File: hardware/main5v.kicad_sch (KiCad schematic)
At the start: 12 parts, among them U701 TPS56837RPAR

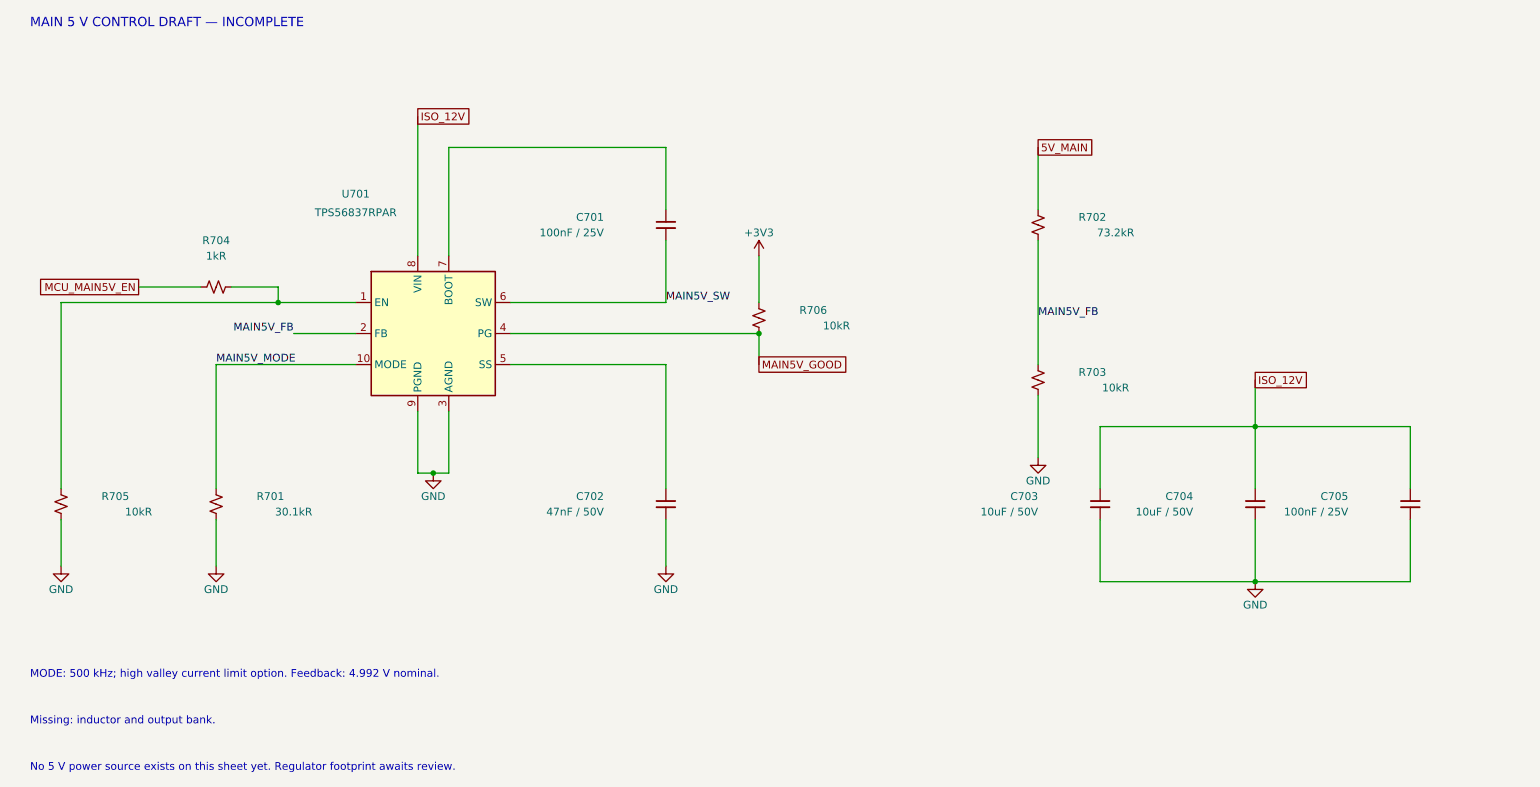
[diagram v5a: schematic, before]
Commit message: Capture main 5 V inductor and local output capacitor bank
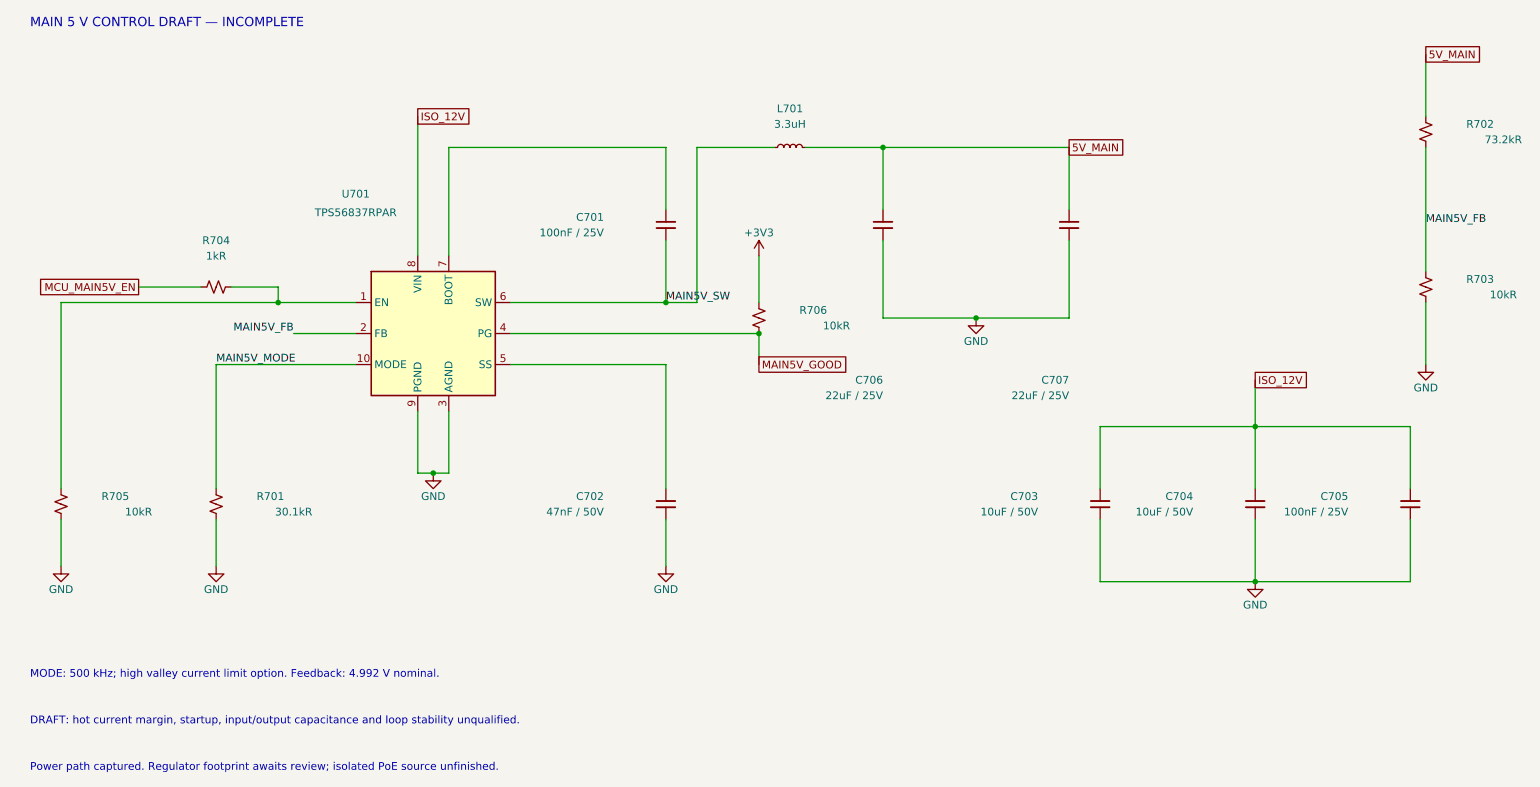
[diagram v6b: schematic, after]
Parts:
- added C706, C707: 22uF / 25V, Capacitor_SMD:C_1210_3225Metric, symbol Device:C_Small
- added L701: 3.3uH, Inductor_SMD:L_Coilcraft_XAL7070-XXX, symbol Device:L_Small
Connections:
- net 5V_MAIN: now also C706.1, C707.1, L701.2
- net GND: now also C706.2, C707.2
- net MAIN5V_SW: now also L701.1
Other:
- note added: "DRAFT: hot current margin, startup, input/output capacitance and loop stability unqualified."
- note added: "Power path captured. Regulator footprint awaits review; isolated PoE source unfinished."
- note removed: "Missing: inductor and output bank."
- note removed: "No 5 V power source exists on this sheet yet. Regulator footprint awaits review."
- moved on the sheet: R702, R703

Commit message: Complete appliance engineering schematic capture
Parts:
- U701: Qualification Footprint pending review; incomplete power path -> Power path captured; RPA land pattern and electrical qualif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
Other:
- note added: "MAIN 5 V CONTROL — ENGINEERING CAPTURE"
- note added: "Power path captured. Regulator footprint, stability and thermal release remain pending."
- note removed: "MAIN 5 V CONTROL DRAFT — INCOMPLETE"
- note removed: "Power path captured. Regulator footprint awaits review; isolated PoE source unfinished."
